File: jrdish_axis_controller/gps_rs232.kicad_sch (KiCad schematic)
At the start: 11 parts, among them CN10 KF2EDGR-2.54-2P, CN11 KF2EDGR-2.54-3P, Q3 BSS138

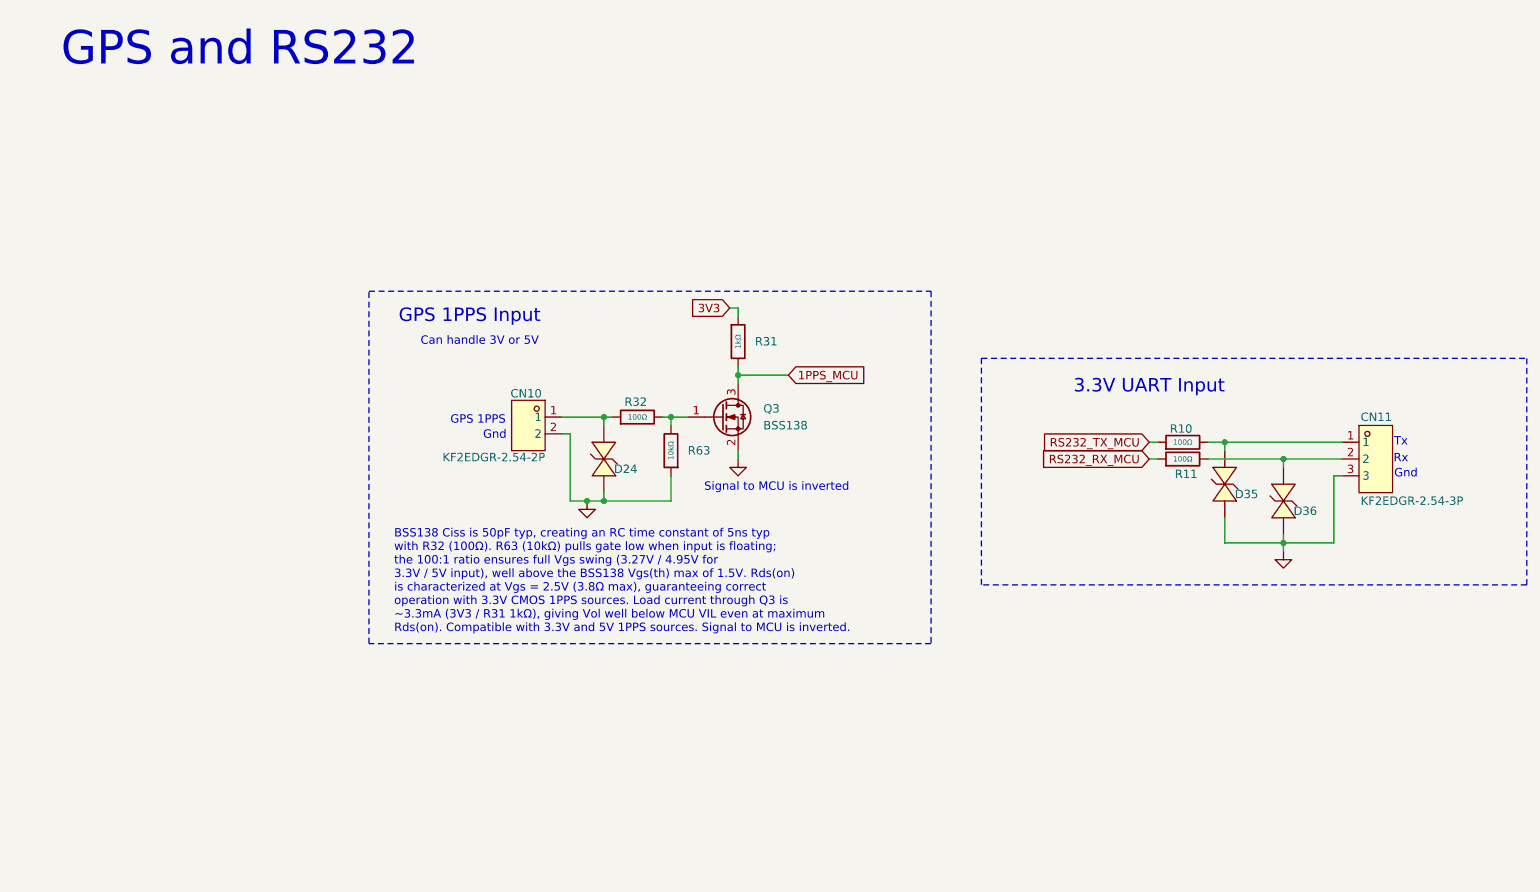
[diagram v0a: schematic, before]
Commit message: Updates for replacing 10k resistors and encoder RC.
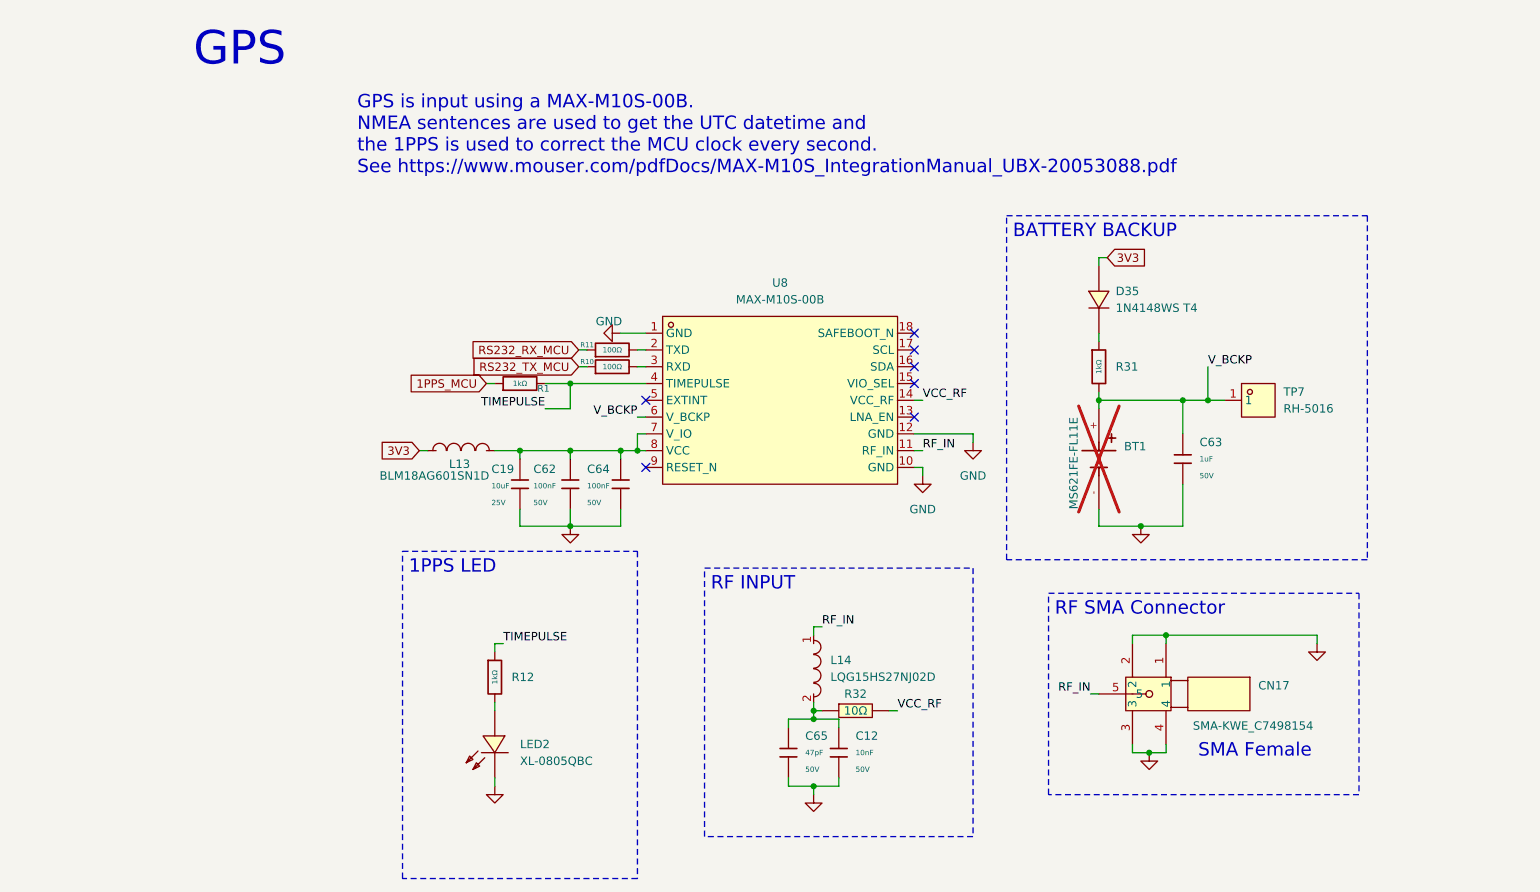
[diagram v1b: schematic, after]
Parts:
- removed CN10: KF2EDGR-2.54-2P, MyParts:CONN-TH_P2.54_KF2EDGR-2.54-2P, symbol MyParts:KF2EDGR-2.54-2P
- removed CN11: KF2EDGR-2.54-3P, MyParts:CONN-TH_3P-P2.54_KF2EDGR-2.54-3P, symbol MyParts:KF2EDGR-2.54-3P
- removed D24, D35, D36: TPESD0402G05V, MyParts:D0402-BI, symbol MyParts:TPESD0402G05V
- removed Q3: BSS138, Package_TO_SOT_SMD:SOT-23, symbol Transistor_FET:BSS138
- removed R31: 1kΩ, PCM_JLCPCB:R_0402, symbol PCM_JLCPCB-Resistors:0402,1kΩ
- removed R32: 100Ω, PCM_JLCPCB:R_0402, symbol PCM_JLCPCB-Resistors:0402,100Ω
- removed R63: 10kΩ, PCM_JLCPCB:R_0402, symbol PCM_JLCPCB-Resistors:0402,10kΩ
- added BT1: MS621FE-FL11E, MyParts:BAT_MS621FE-FL11E, symbol MyParts:MS621FE-FL11E
- added C12: 10nF, PCM_JLCPCB:C_0603, symbol PCM_JLCPCB-Capacitors:0603,10nF
- added C19: 10uF, PCM_JLCPCB:C_0603, symbol PCM_JLCPCB-Capacitors:0603,10uF,(2)
- added C62, C64: 100nF, PCM_JLCPCB:C_0603, symbol PCM_JLCPCB-Capacitors:0603,100nF
- added C63: 1uF, PCM_JLCPCB:C_0603, symbol PCM_JLCPCB-Capacitors:0603,1uF
- added C65: 47pF, PCM_JLCPCB:C_0603, symbol PCM_JLCPCB-Capacitors:0603,47pF
- added CN17: SMA-KWE_C7498154, MyParts:SMA-TH_SMA-KWE_C7498154, symbol MyParts:SMA-KWE_C7498154
- added D35: 1N4148WS T4, MyParts:SOD-323_L1.8-W1.3-LS2.5-RD, symbol MyParts:1N4148WST4
- added L13: BLM18AG601SN1D, MyParts:L0603, symbol MyParts:BLM18AG601SN1D
- added L14: LQG15HS27NJ02D, MyParts:L0402-RD, symbol MyParts:LQG15HS27NJ02D
- added LED2: XL-0805QBC, MyParts:LED0805-R-RD, symbol MyParts:XL-0805QBC
- added R1: 1kΩ, PCM_JLCPCB:R_0402, symbol PCM_JLCPCB-Resistors:0402,1kΩ
- added R12, R31: 1kΩ, PCM_JLCPCB:R_0603, symbol PCM_JLCPCB-Resistors:0603,1kΩ
- added R32: 10Ω, MyParts:R1206, symbol MyParts:1206W4F100JT5E
- added TP7: RH-5016, MyParts:TESTPOINT-SMD_L3.0-W2.0, symbol MyParts:RH-5016
- added U8: MAX-M10S-00B, MyParts:SMD-18_L10.1-W9.7-P1.10-TL_SKG09F, symbol MyParts:MAX-M10S-00B
- R10, R11: Field4 (none) -> ${REFERENCE}
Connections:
- net 1PPS_MCU: now also R1.1
- net 3V3: now also D35.2 (A), L13.1
- net GND: now also BT1.-, C12.2, C19.2, C62.2, C63.2, C64.2, C65.2, CN17.1, CN17.2, CN17.3, CN17.4, LED2.2 (K), U8.1 (GND), U8.10 (GND), U8.12 (GND)
- net at R11.2: now also U8.2 (TXD)
- net at R10.2: now also U8.3 (RXD)
- new net: LED2.1 (A), R12.2
- new net: C19.1, C62.1, C64.1, L13.2, U8.7 (V_IO), U8.8 (VCC)
- new net: C12.1, C65.1, L14.2, R32.1
- new net: D35.1 (K), R31.1
- new net RF_IN: CN17.5, L14.1, U8.11 (RF_IN)
- new net TIMEPULSE: R1.2, R12.1, U8.4 (TIMEPULSE)
- new net VCC_RF: R32.2, U8.14 (VCC_RF)
- new net V_BCKP: BT1.+, C63.1, R31.2, TP7.1, U8.6 (V_BCKP)
- no-connect marks 0 -> 7
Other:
- note added: "GPS"
- note added: "GPS is input using a MAX-M10S-00B. NMEA sentences are used to get the UTC datetime and the 1PPS is used to correct the MCU clock every second. See https://www.mouser.com/pdfDocs/MAX-M10S_IntegrationManual_UBX-20053088.pdf"
- note added: "SMA Female"
- note removed: "3.3V UART Input"
- note removed: "BSS138 Ciss is 50pF typ, creating an RC time constant of 5ns typ with R32 (100Ω). R63 (10kΩ) pulls gate low when input is floating; the 100:1 ratio ensures full Vgs swing (3.27V / 4.95V for 3.3V / 5V input), well above the BSS138 Vgs(th) max of 1.5V. Rds(on) is characterized at Vgs = 2.5V (3.8Ω max), guaranteeing correct operation with 3.3V CMOS 1PPS sources. Load current through Q3 is ~3.3mA (3V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"
- note removed: "Can handle 3V or 5V"
- note removed: "GPS 1PPS"
- note removed: "GPS 1PPS Input"
- note removed: "GPS and RS232"
- note removed: "Gnd"
- note removed: "Rx"
- note removed: "Signal to MCU is inverted"
- note removed: "Tx"
- moved on the sheet: R10, R11
